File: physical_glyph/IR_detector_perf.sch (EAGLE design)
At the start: 20 parts, among them IC1 7805T, T1 BP103, U1 MCP6004-I/P, U2 LM339PWR

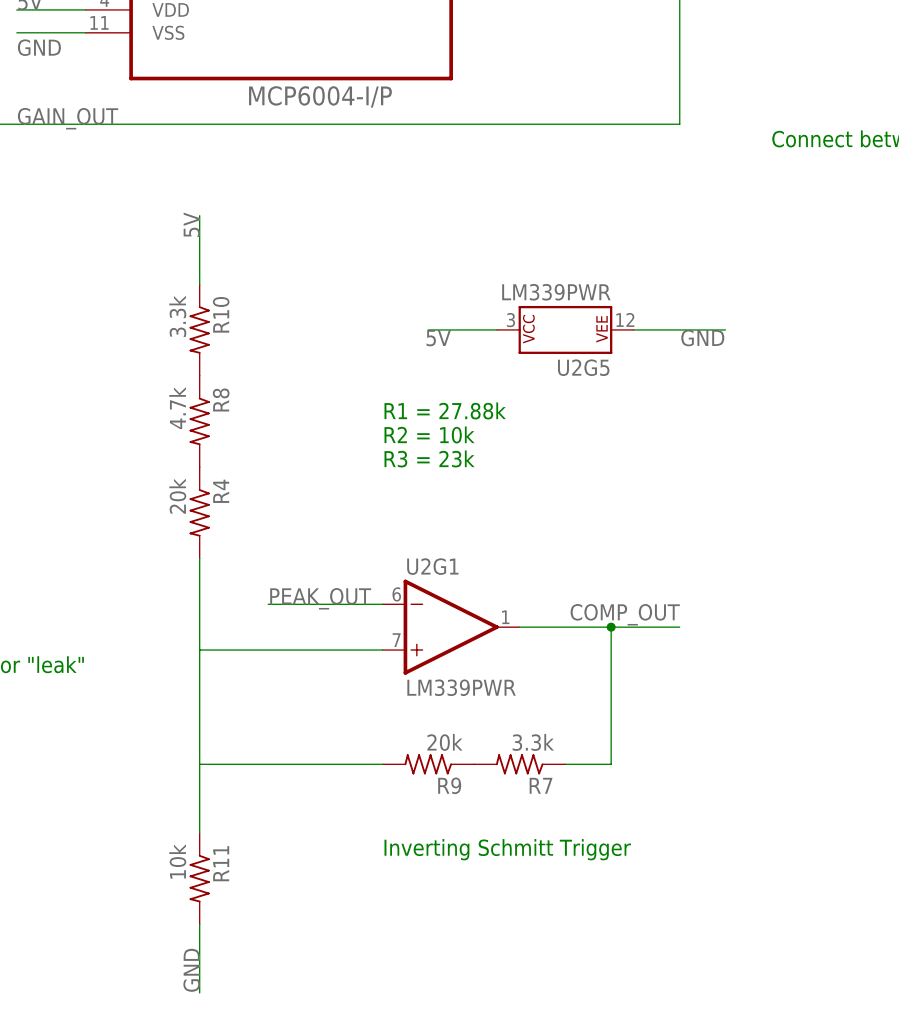
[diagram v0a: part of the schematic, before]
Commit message: Fix inverted Schmitt Trigger
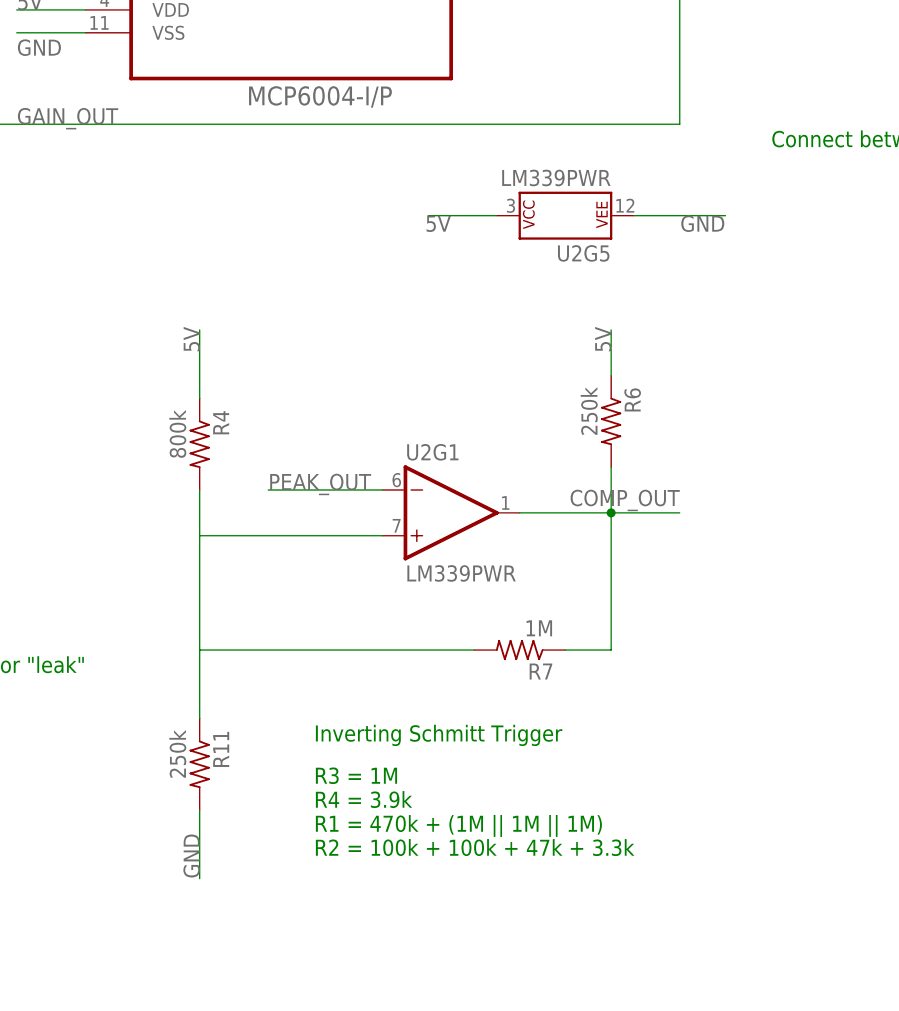
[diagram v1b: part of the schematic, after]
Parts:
- removed R10: 3.3k, rcl:R-US_0204/2V
- removed R8: 4.7k, rcl:R-US_0204/2V
- removed R9: 20k, rcl:R-US_0204/2V
- added R6: 250k, rcl:R-US_0204/2V
- R11: value 10k -> 250k
- R4: value 20k -> 800k
- R7: value 3.3k -> 1M
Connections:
- removed net N$1: R10.2, R8.1
- removed net N$2: R7.2, R9.1
- removed net N$4: R4.1, R8.2
- net 5V: now also R4.1, R6.1; no longer R10.1
- net COMP_OUT: now also R6.2
- net N$34: now also R7.2; no longer R9.2
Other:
- note added: "R3 = 1M R4 = 3.9k R1 = 470k + (1M || 1M || 1M) R2 = 100k + 100k + 47k + 3.3k"
- note removed: "R1 = 27.88k R2 = 10k R3 = 23k"
- moved on the sheet: R11, R4, R7, U2G1, U2G5

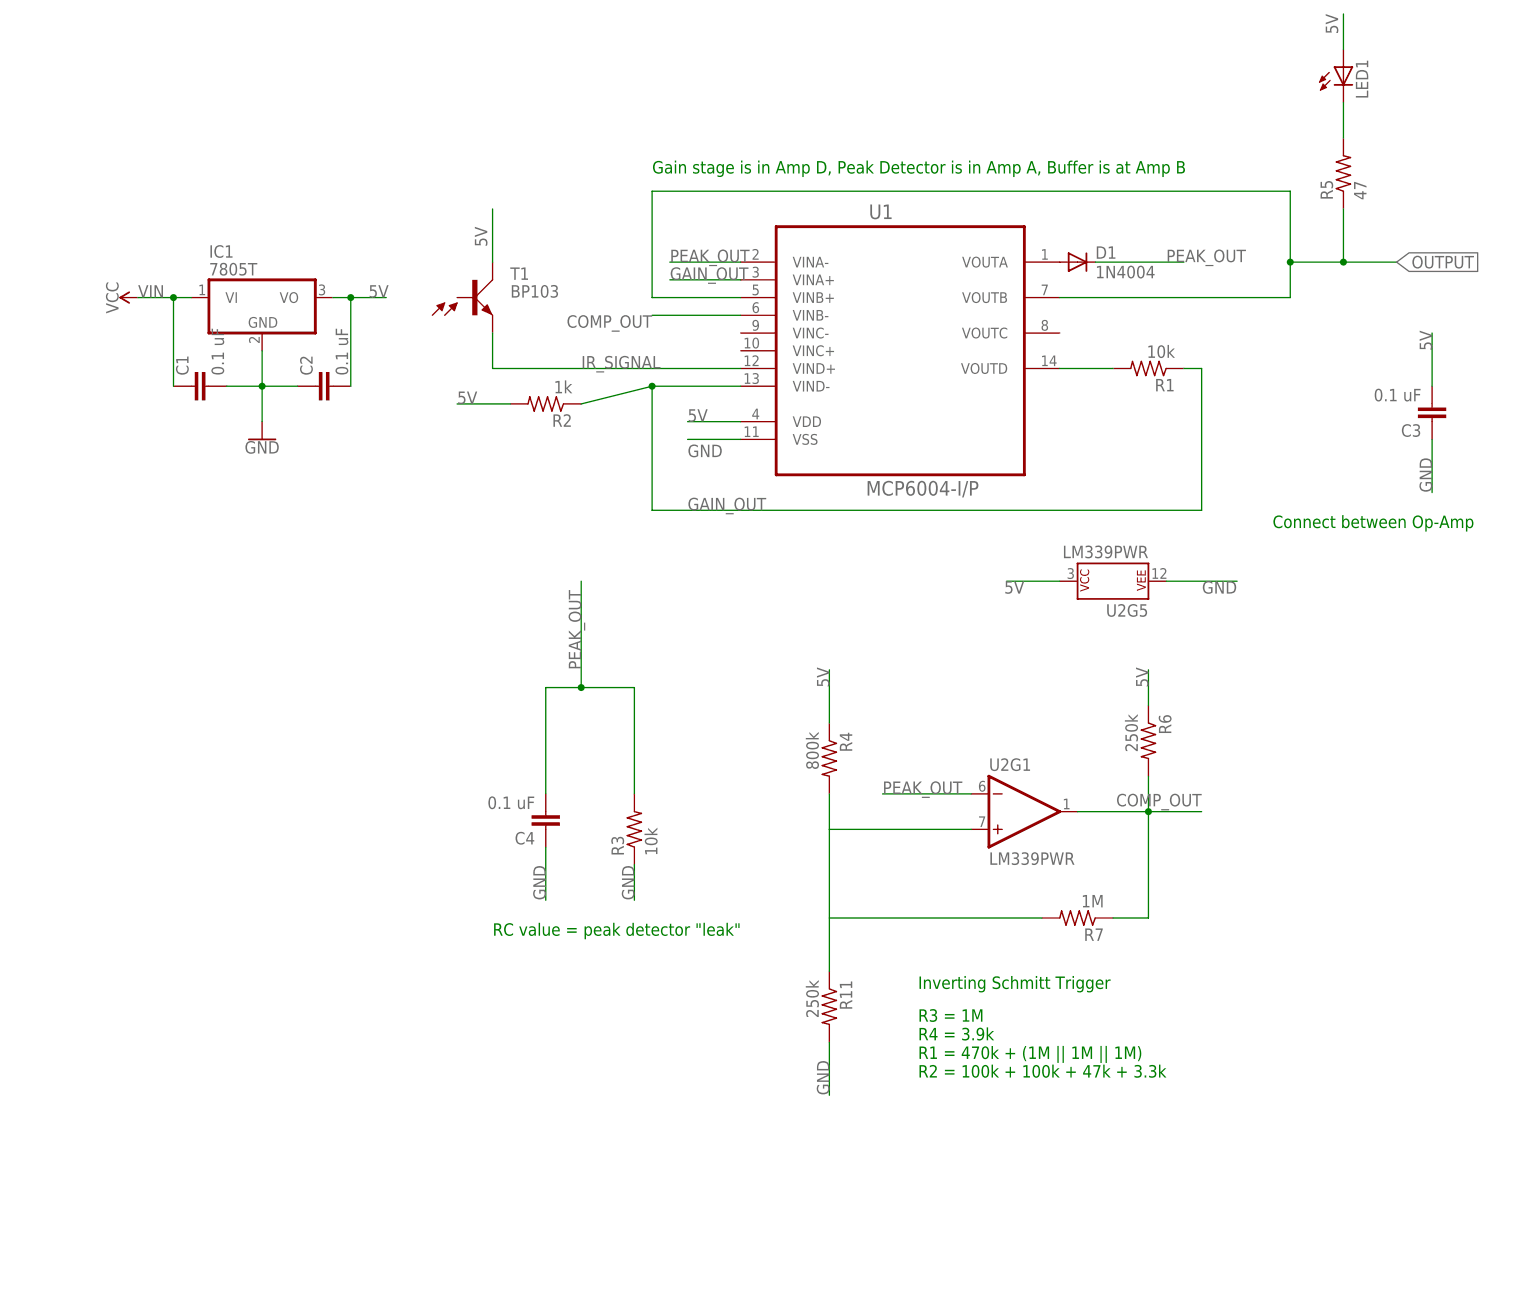
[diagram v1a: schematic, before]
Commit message: Remove unneeded buffer
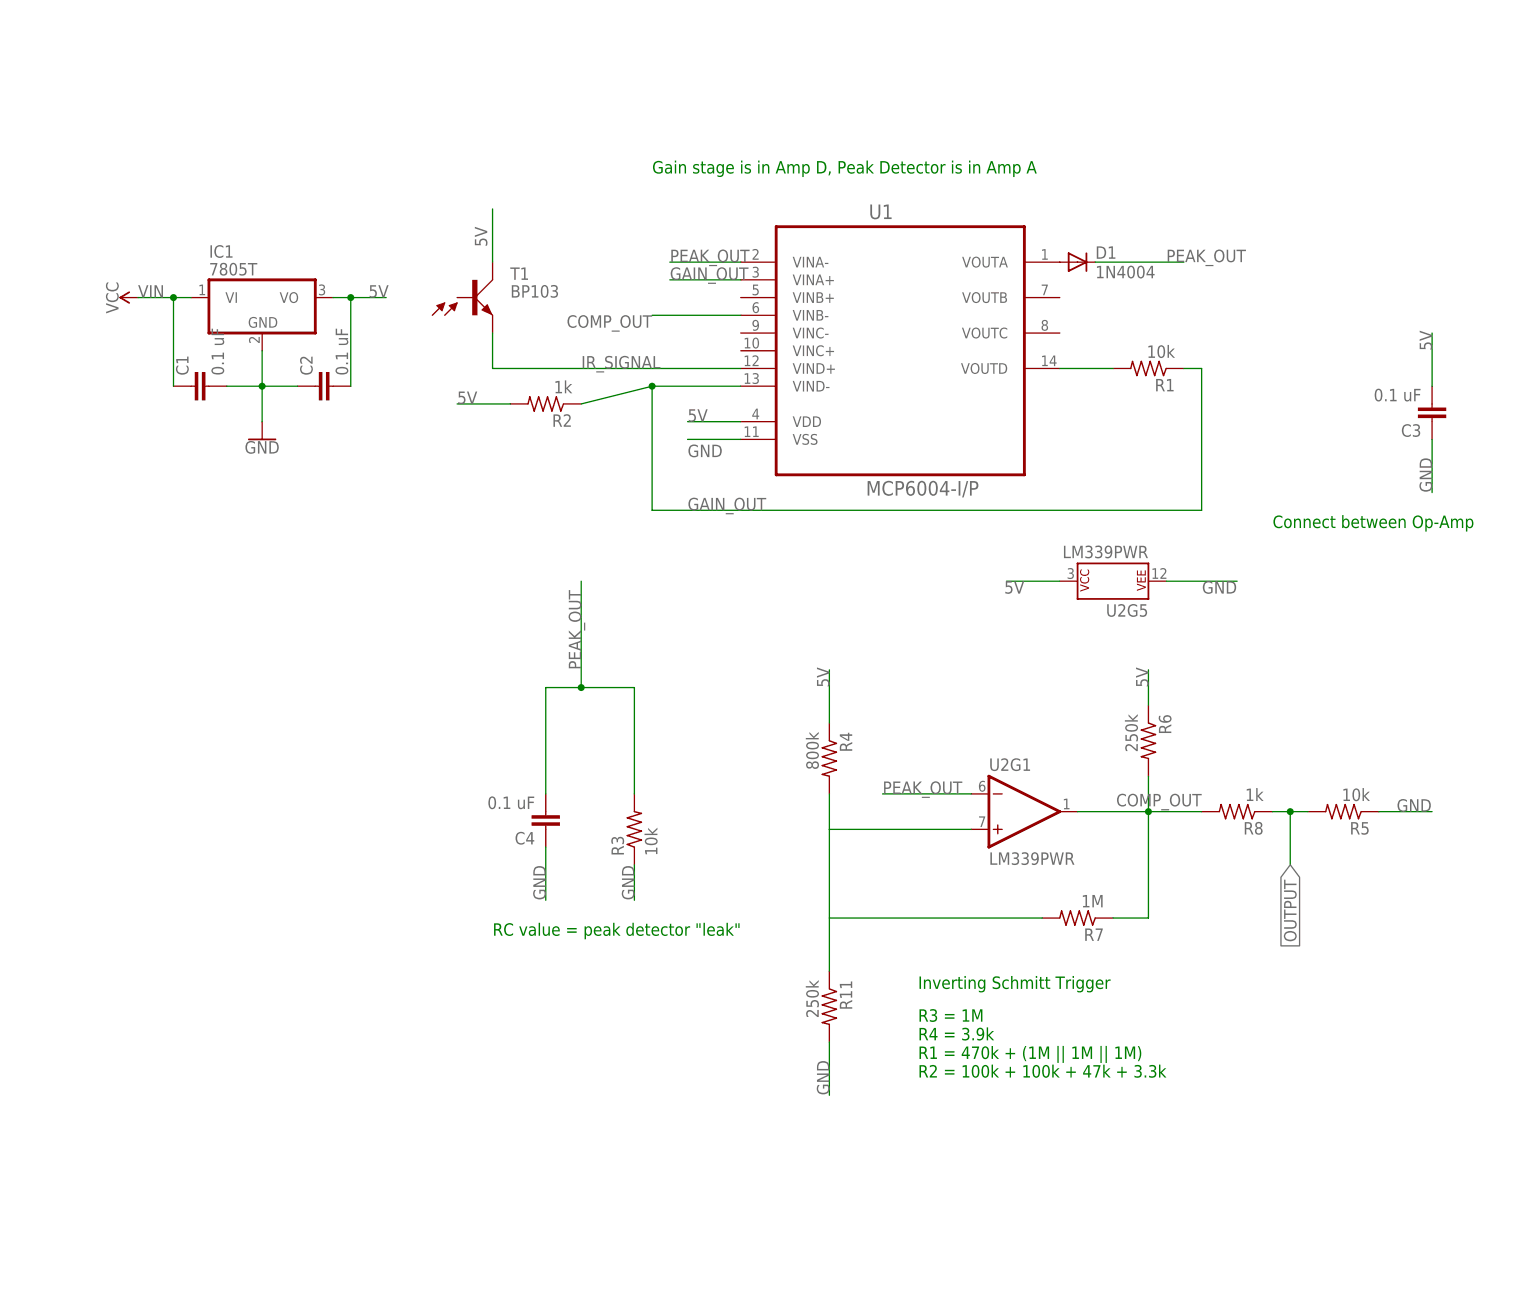
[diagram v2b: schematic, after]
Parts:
- removed LED1: (no value), led:LED5MM
- added R8: 1k, rcl:R-US_0204/2V
- R5: value 47 -> 10k
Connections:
- removed net N$5: LED1.C, R5.2
- net 5V: no longer LED1.A
- net COMP_OUT: now also R8.2
- net GND: now also R5.1
- net OUTPUT: now also R5.2, R8.1; no longer R5.1, U1.VINB+, U1.VOUTB
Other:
- note added: "Gain stage is in Amp D, Peak Detector is in Amp A"
- note removed: "Gain stage is in Amp D, Peak Detector is in Amp A, Buffer is at Amp B"
- moved on the sheet: R5
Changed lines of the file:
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@@
 <part name="R3" library="rcl" library_urn="urn:adsk.eagle:library:334" deviceset="R-US_" device="0204/2V" package3d_urn="urn:adsk.eagle:package:23495/1" value="10k"/>
 <part name="R4" library="rcl" library_urn="urn:adsk.eagle:library:334" deviceset="R-US_" device="0204/2V" package3d_urn="urn:adsk.eagle:package:23495/1" value="800k"/>
-<part name="R5" library="rcl" library_urn="urn:adsk.eagle:library:334" deviceset="R-US_" device="0204/2V" package3d_urn="urn:adsk.eagle:package:23495/1" value="47"/>
 <part name="R7" library="rcl" library_urn="urn:adsk.eagle:library:334" deviceset="R-US_" device="0204/2V" package3d_urn="urn:adsk.eagle:package:23495/1" value="1M"/>
 <part name="R11" library="rcl" library_urn="urn:adsk.eagle:library:334" deviceset="R-US_" device="0204/2V" package3d_urn="urn:adsk.eagle:package:23495/1" value="250k"/>
-<part name="LED1" library="led" library_urn="urn:adsk.eagle:library:259" deviceset="LED" device="5MM" package3d_urn="urn:adsk.eagle:package:15799/2"/>
 <part name="C3" library="resistor" library_urn="urn:adsk.eagle:library:348" deviceset="C-EU" device="025-024X044" package3d_urn="urn:adsk.eagle:package:26149/1" value="0.1 uF"/>
 <part name="C4" library="resistor" library_urn="urn:adsk.eagle:library:348" deviceset="C-EU" device="025-024X044" package3d_urn="urn:adsk.eagle:package:26149/1" value="0.1 uF"/>
 <part name="U2" library="SparkFun-IC-Amplifiers" deviceset="LM339" device="" value="LM339PWR"/>
 <part name="R6" library="rcl" library_urn="urn:adsk.eagle:library:334" deviceset="R-US_" device="0204/2V" package3d_urn="urn:adsk.eagle:package:23495/1" value="250k"/>
+<part name="R5" library="rcl" library_urn="urn:adsk.eagle:library:334" deviceset="R-US_" device="0204/2V" package3d_urn="urn:adsk.eagle:package:23495/1" value="10k"/>
+<part name="R8" library="rcl" library_urn="urn:adsk.eagle:library:334" deviceset="R-US_" device="0204/2V" package3d_urn="urn:adsk.eagle:package:23495/1" value="1k"/>
 </parts>
 <sheets>
@@
 <plain>
 <text x="129.54" y="50.8" size="1.778" layer="91">Connect between Op-Amp</text>
-<text x="40.64" y="101.6" size="1.778" layer="91">Gain stage is in Amp D, Peak Detector is in Amp A, Buffer is at Amp B</text>
+<text x="40.64" y="101.6" size="1.778" layer="91">Gain stage is in Amp D, Peak Detector is in Amp A</text>
 <text x="78.74" y="-27.94" size="1.778" layer="91">R3 = 1M
 R4 = 3.9k
@@
 <instance part="R3" gate="G$1" x="38.1" y="7.62" rot="R90"/>
 <instance part="R4" gate="G$1" x="66.04" y="17.78" rot="R270"/>
-<instance part="R5" gate="G$1" x="139.7" y="101.6" rot="R90"/>
 <instance part="R7" gate="G$1" x="101.6" y="-5.08" rot="R180"/>
 <instance part="R11" gate="G$1" x="66.04" y="-17.78" rot="R270"/>
-<instance part="LED1" gate="G$1" x="139.7" y="116.84"/>
 <instance part="C3" gate="G$1" x="152.4" y="66.04" rot="R180"/>
 <instance part="C4" gate="G$1" x="25.4" y="7.62" rot="R180"/>
@@
 <instance part="U2" gate="G5" x="106.68" y="43.18" rot="R90"/>
 <instance part="R6" gate="G$1" x="111.76" y="20.32" rot="R270"/>
+<instance part="R5" gate="G$1" x="139.7" y="10.16" rot="R180"/>
+<instance part="R8" gate="G$1" x="124.46" y="10.16" rot="R180"/>
 </instances>
 <busses>
@@
 <wire x1="17.78" y1="88.9" x2="17.78" y2="96.52" width="0.1524" layer="91"/>
 <label x="15.24" y="93.98" size="1.778" layer="95" rot="R270"/>
-</segment>
-<segment>
-<pinref part="LED1" gate="G$1" pin="A"/>
-<wire x1="139.7" y1="119.38" x2="139.7" y2="124.46" width="0.1524" layer="91"/>
-<label x="137.16" y="124.46" size="1.778" layer="95" rot="R270"/>
 </segment>
 <segment>
@@
 <label x="66.04" y="-30.48" size="1.778" layer="95" rot="R90"/>
 </segment>
+<segment>
+<pinref part="R5" gate="G$1" pin="1"/>
+<wire x1="144.78" y1="10.16" x2="152.4" y2="10.16" width="0.1524" layer="91"/>
+<label x="147.32" y="10.16" size="1.778" layer="95"/>
+</segment>
 </net>
 <net name="IR_SIGNAL" class="0">
@@
 <wire x1="17.78" y1="73.66" x2="53.34" y2="73.66" width="0.1524" layer="91"/>
 <label x="30.48" y="73.66" size="1.778" layer="95"/>
-</segment>
-</net>
-<net name="N$5" class="0">
-<segment>
-<pinref part="LED1" gate="G$1" pin="C"/>
-<wire x1="139.7" y1="111.76" x2="139.7" y2="106.68" width="0.1524" layer="91"/>
-<pinref part="R5" gate="G$1" pin="2"/>
 </segment>
 </net>
@@
 <pinref part="R6" gate="G$1" pin="2"/>
 <wire x1="111.76" y1="15.24" x2="111.76" y2="10.16" width="0.1524" layer="91"/>
+<pinref part="R8" gate="G$1" pin="2"/>
 </segment>
 </net>
 <net name="OUTPUT" class="0">
 <segment>
-<pinref part="U1" gate="A" pin="VINB+"/>
-<wire x1="53.34" y1="83.82" x2="40.64" y2="83.82" width="0.1524" layer="91"/>
-<wire x1="40.64" y1="83.82" x2="40.64" y2="99.06" width="0.1524" layer="91"/>
-<wire x1="40.64" y1="99.06" x2="132.08" y2="99.06" width="0.1524" layer="91"/>
-<label x="147.32" y="88.9" size="1.778" layer="95" xref="yes"/>
-<pinref part="R5" gate="G$1" pin="1"/>
-<wire x1="132.08" y1="88.9" x2="139.7" y2="88.9" width="0.1524" layer="91"/>
-<wire x1="139.7" y1="88.9" x2="139.7" y2="96.52" width="0.1524" layer="91"/>
-<wire x1="132.08" y1="99.06" x2="132.08" y2="88.9" width="0.1524" layer="91"/>
-<wire x1="132.08" y1="88.9" x2="132.08" y2="83.82" width="0.1524" layer="91"/>
-<junction x="132.08" y="88.9"/>
-<pinref part="U1" gate="A" pin="VOUTB"/>
-<wire x1="132.08" y1="83.82" x2="99.06" y2="83.82" width="0.1524" layer="91"/>
-<wire x1="139.7" y1="88.9" x2="147.32" y2="88.9" width="0.1524" layer="91"/>
-<junction x="139.7" y="88.9"/>
-</segment>
-</net>
+<label x="132.08" y="2.54" size="1.778" layer="95" rot="R270" xref="yes"/>
+<wire x1="132.08" y1="10.16" x2="132.08" y2="2.54" width="0.1524" layer="91"/>
+<pinref part="R8" gate="G$1" pin="1"/>
+<wire x1="129.54" y1="10.16" x2="132.08" y2="10.16" width="0.1524" layer="91"/>
+<pinref part="R5" gate="G$1" pin="2"/>
+<wire x1="132.08" y1="10.16" x2="134.62" y2="10.16" width="0.1524" layer="91"/>
+<junction x="132.08" y="10.16"/>
+</segment>
+</net>
